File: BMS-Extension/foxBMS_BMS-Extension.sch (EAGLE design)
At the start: 219 parts, among them IC1001 AQV252G2S, IC1002 AQV252G2S, IC1003 AQV252G2S, IC1101 UA78L05ACPK, IC1102 ADUM1300ARW, IC1301 UA78L05ACPK, IC1302 LTC485CS8#PBF, IC1303 ADUM1401ARW, IC1701 ADR3425ARJZ, IC1901 UA78L05ACPK, IC1902 ADUM1402ARW, IC1903 ADUM1402ARW, IC2001 AQV25G2S, IC2002 AQV25G2S, IC2003 AQV25G2S, IC2004 AQV25G2S, IC2005 AQV25G2S, IC2006 AQV25G2S, IC801 KA7805ERTF, IC802 CPC1008N, IC803 TJA1052IT/1Y, T1001 IRLML0100TRPBF, T1002 IRLML0100TRPBF, T1003 IRLML0100TRPBF, T1501 BSS84P, T2001 IRLML0100TRPBF, T2002 IRLML0100TRPBF, T2003 IRLML0100TRPBF, T2004 IRLML0100TRPBF, T2005 IRLML0100TRPBF, T2006 IRLML0100TRPBF, T801 IRLML0100TRPBF, T901 BUK964R8-60E, X1201 43045-0400_MOLEX_4PIN, X1202 43045-0400_MOLEX_4PIN, X1203 43045-0400_MOLEX_4PIN, X1301 43045-0600_MOLEX_6PIN, X1701 43045-1200_MOLEX_12PIN, X1901 43045-1000_MOLEX_10PIN, X2001 43045-1200_MOLEX_12PIN, X801 43045-0400_MOLEX_4PIN

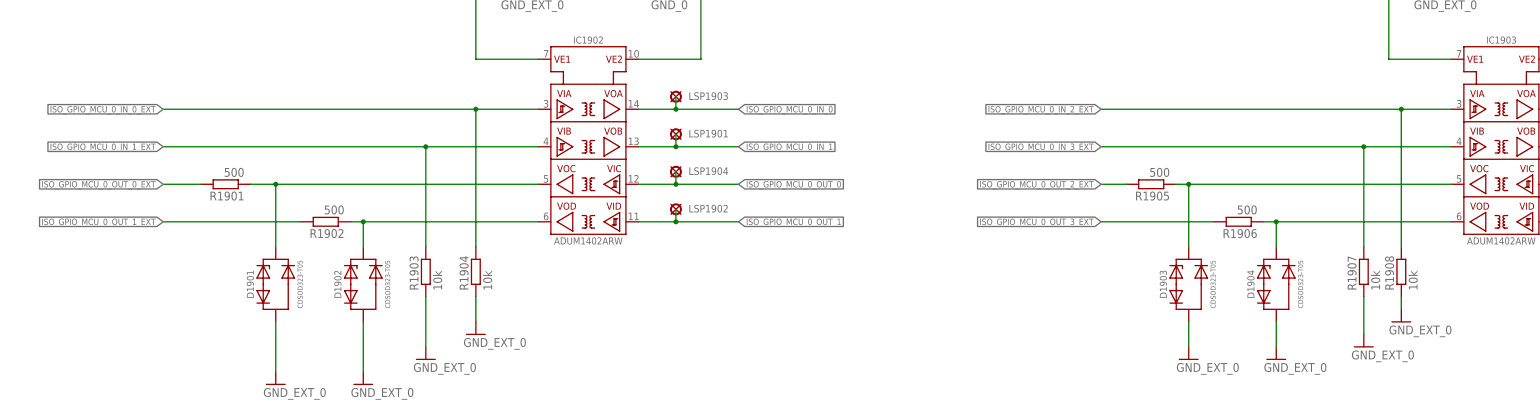
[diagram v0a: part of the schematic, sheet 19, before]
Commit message: Minor updates and corrections of notations, wording and bill of materials (V1.0.1). No changes in schematic and layout.
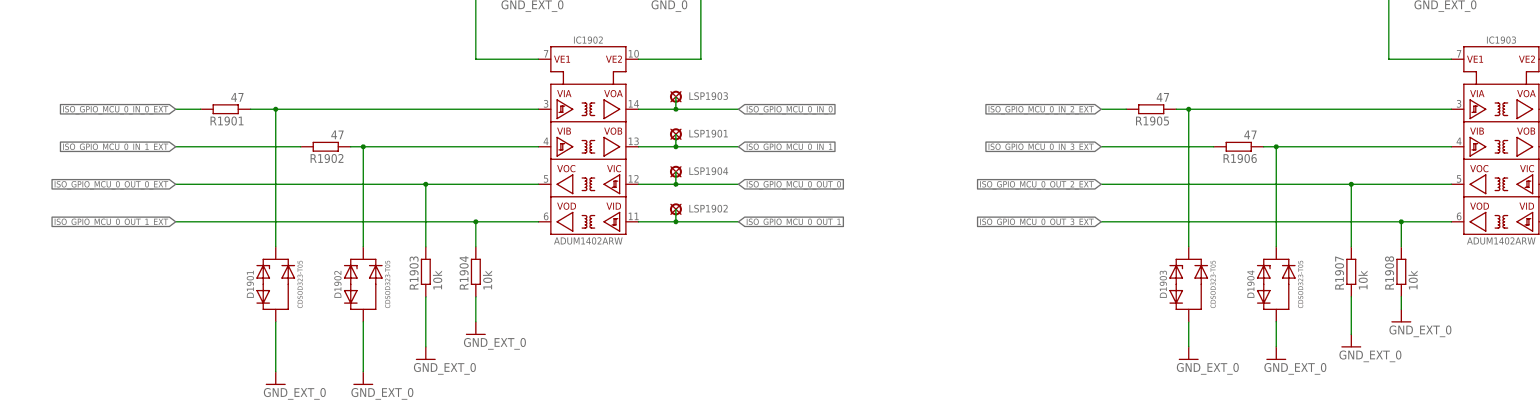
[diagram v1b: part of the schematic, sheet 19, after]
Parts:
- R1101, R1102, R1103, R1901, R1902, R1905, R1906: value 500 -> 47
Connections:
- removed net N$24: D1901.C, IC1902G$1.VOC, R1901.1
- removed net N$25: D1902.C, IC1902G$1.VOD, R1902.1
- removed net N$26: D1903.C, IC1903G$1.VOC, R1905.1
- removed net N$27: D1904.C, IC1903G$1.VOD, R1906.1
- new net N$1111: D1903.C, IC1903G$1.VIA, R1905.1
- new net N$254548: D1904.C, IC1903G$1.VIB, R1906.1
- new net N$5555: D1901.C, IC1902G$1.VIA, R1901.1
- new net N$7555: D1902.C, IC1902G$1.VIB, R1902.1
- net ISO_GPIO_MCU_0_IN_0_EXT: now also R1901.2; no longer R1904.2
- net ISO_GPIO_MCU_0_IN_1_EXT: now also R1902.2; no longer IC1902G$1.VIB, R1903.2
- net ISO_GPIO_MCU_0_IN_2_EXT: now also R1905.2; no longer IC1903G$1.VIA, R1908.2
- net ISO_GPIO_MCU_0_IN_3_EXT: now also R1906.2; no longer IC1903G$1.VIB, R1907.2
- net ISO_GPIO_MCU_0_OUT_0_EXT: now also IC1902G$1.VOC, R1903.2; no longer R1901.2
- net ISO_GPIO_MCU_0_OUT_1_EXT: now also IC1902G$1.VOD, R1904.2; no longer R1902.2
- net ISO_GPIO_MCU_0_OUT_2_EXT: now also IC1903G$1.VOC, R1907.2; no longer R1905.2
- net ISO_GPIO_MCU_0_OUT_3_EXT: now also IC1903G$1.VOD, R1908.2; no longer R1906.2
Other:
- note added: "Connectors to BMS-Master"
- note added: "This page was intentionally left blank."
- note removed: "Connectors to Basic Board"
- note removed: "Please Note: As the foxBMS BMS-Master was designed as one unit, the schematic of BMS-Master Basic or Extension may include blank pages."
- moved on the sheet: R1901, R1902, R1905, R1906, R1907

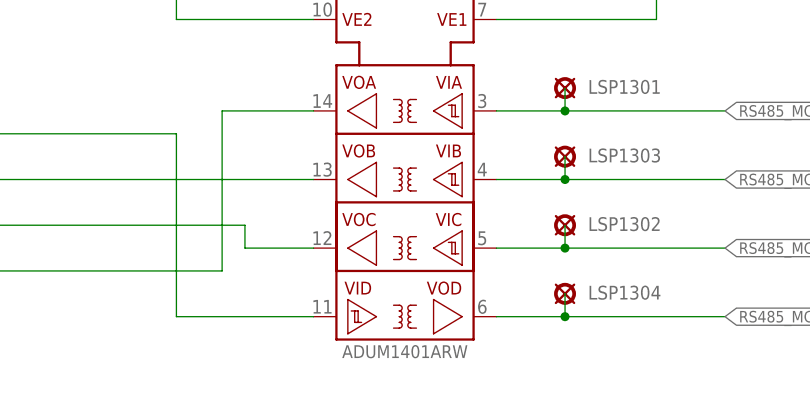
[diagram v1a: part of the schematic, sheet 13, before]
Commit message: Changed ADUM1xxx to ADUM3xxx in schematic of BMS-Master and BMS-Extension
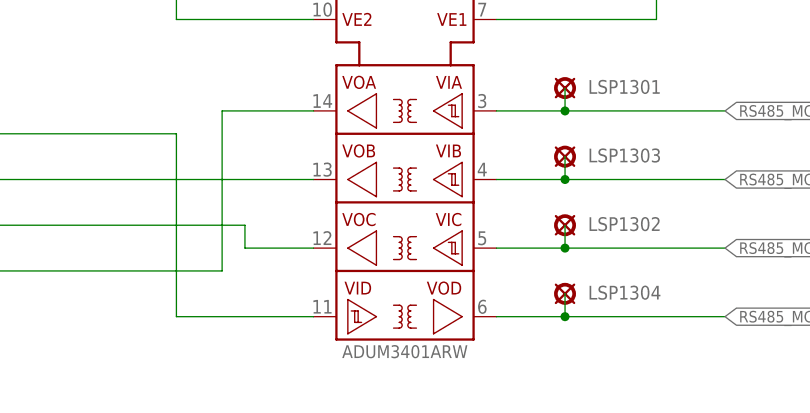
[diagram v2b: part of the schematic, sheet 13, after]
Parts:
- IC1102: value ADUM1300ARW -> ADUM3300ARW; device 0_LES_SCHNITTSTELLEN-IC.SMD.ISOLATOR:ADUM1300ARW -> foxBMS_BMS-Master:ADUM3300ARW
- IC1303: value ADUM1401ARW -> ADUM3401ARW; device 0_LES_SCHNITTSTELLEN-IC.SMD.ISOLATOR:ADUM1401ARW -> foxBMS_BMS-Master:ADUM3401ARW
- IC1902, IC1903: value ADUM1402ARW -> ADUM3402ARW; device 0_LES_SCHNITTSTELLEN-IC.SMD.ISOLATOR:ADUM1402ARW -> foxBMS_BMS-Extension:ADUM3402ARW

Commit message: updated foxBMS-slave to version 2.02
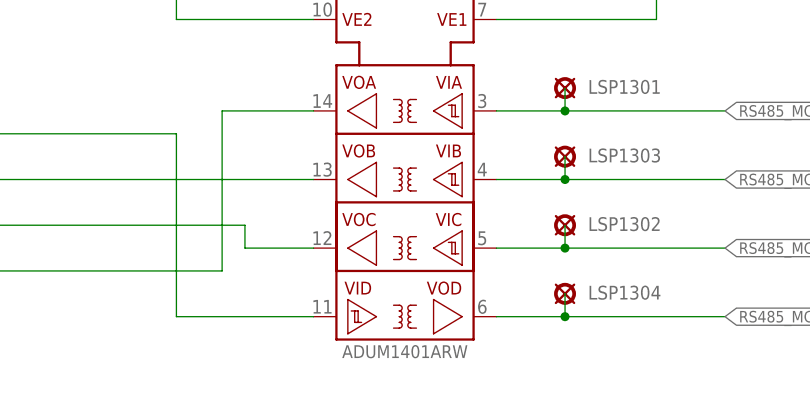
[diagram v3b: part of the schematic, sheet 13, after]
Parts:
- IC1102: value ADUM3300ARW -> ADUM1300ARW; device foxBMS_BMS-Master:ADUM3300ARW -> 0_LES_SCHNITTSTELLEN-IC.SMD.ISOLATOR:ADUM1300ARW
- IC1303: value ADUM3401ARW -> ADUM1401ARW; device foxBMS_BMS-Master:ADUM3401ARW -> 0_LES_SCHNITTSTELLEN-IC.SMD.ISOLATOR:ADUM1401ARW
- IC1902, IC1903: value ADUM3402ARW -> ADUM1402ARW; device foxBMS_BMS-Extension:ADUM3402ARW -> 0_LES_SCHNITTSTELLEN-IC.SMD.ISOLATOR:ADUM1402ARW
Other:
- note added: "Connectors to Basic Board"
- note added: "Please Note: As the foxBMS BMS-Master was designed as one unit, the schematic of BMS-Master Basic or Extension may include blank pages."
- note removed: "Connectors to BMS-Master"
- note removed: "This page was intentionally left blank."
